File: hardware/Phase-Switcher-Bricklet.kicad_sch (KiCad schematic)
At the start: 42 parts, among them CN1 HC-GH-7PWTKK, P1 WJ124-3.81-2P, P2 WJ124-3.81-6P, P3 WJ124-3.81-6P, U1 XMC1302-Q024X0032-AB, U2 AQY282SX, U3 AQH3213A, U4 HCPL2731S, U5 AQH3213A, U6 HCPL2731S

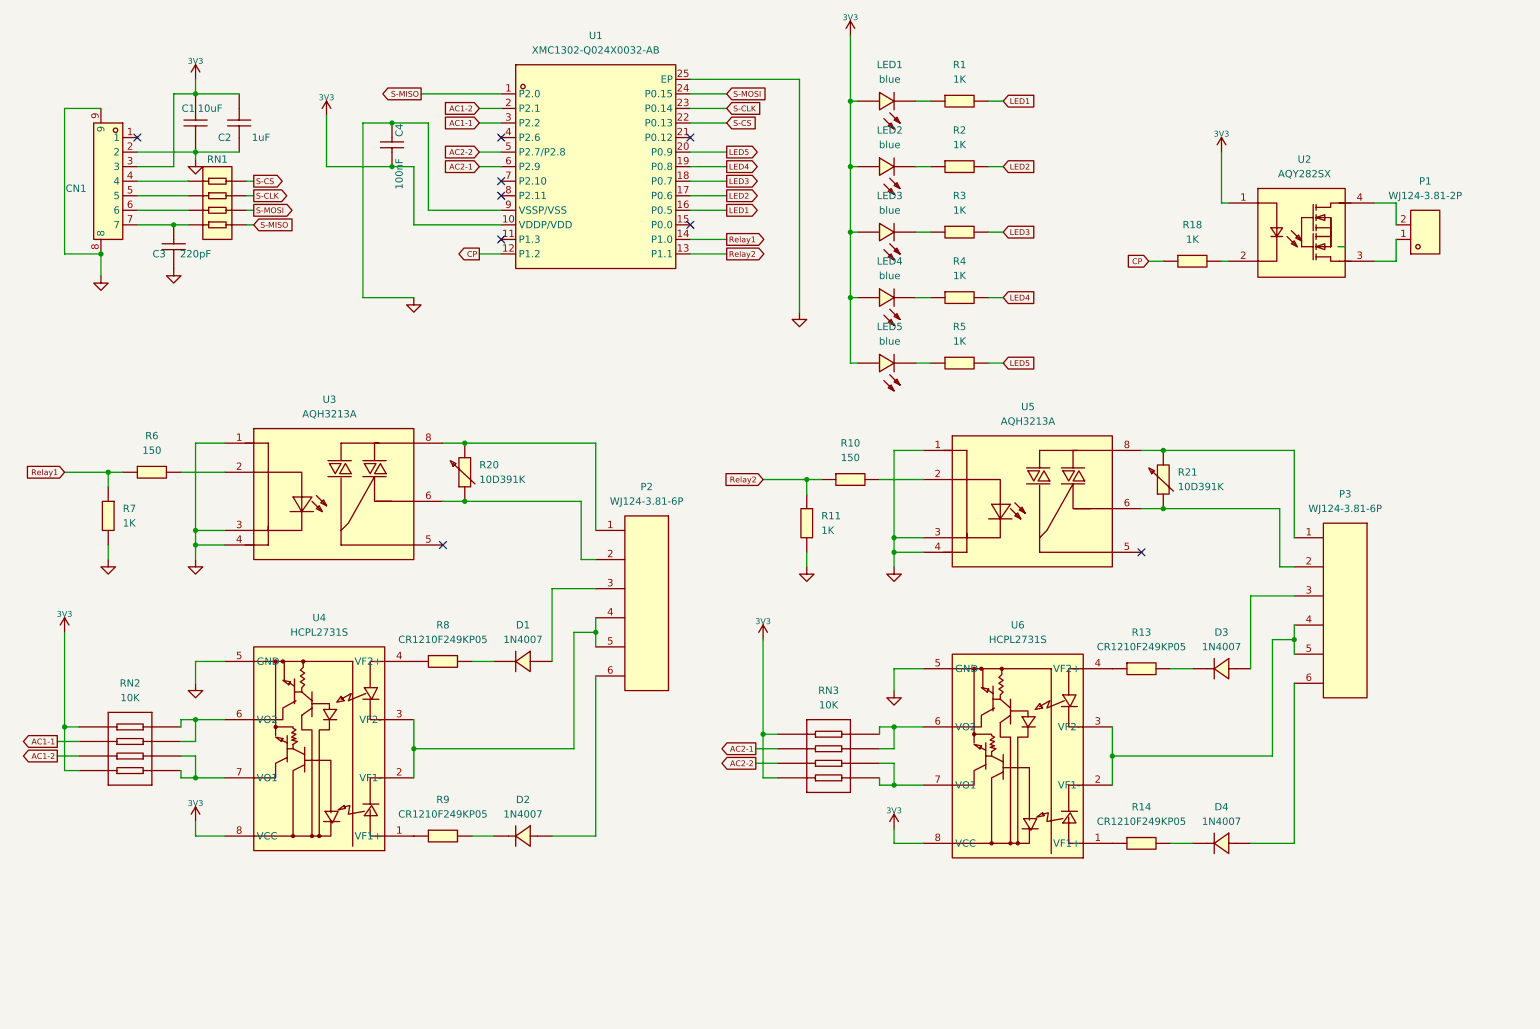
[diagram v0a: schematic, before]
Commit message: Phase-Switcher-Bricklet: Rev. 1.1
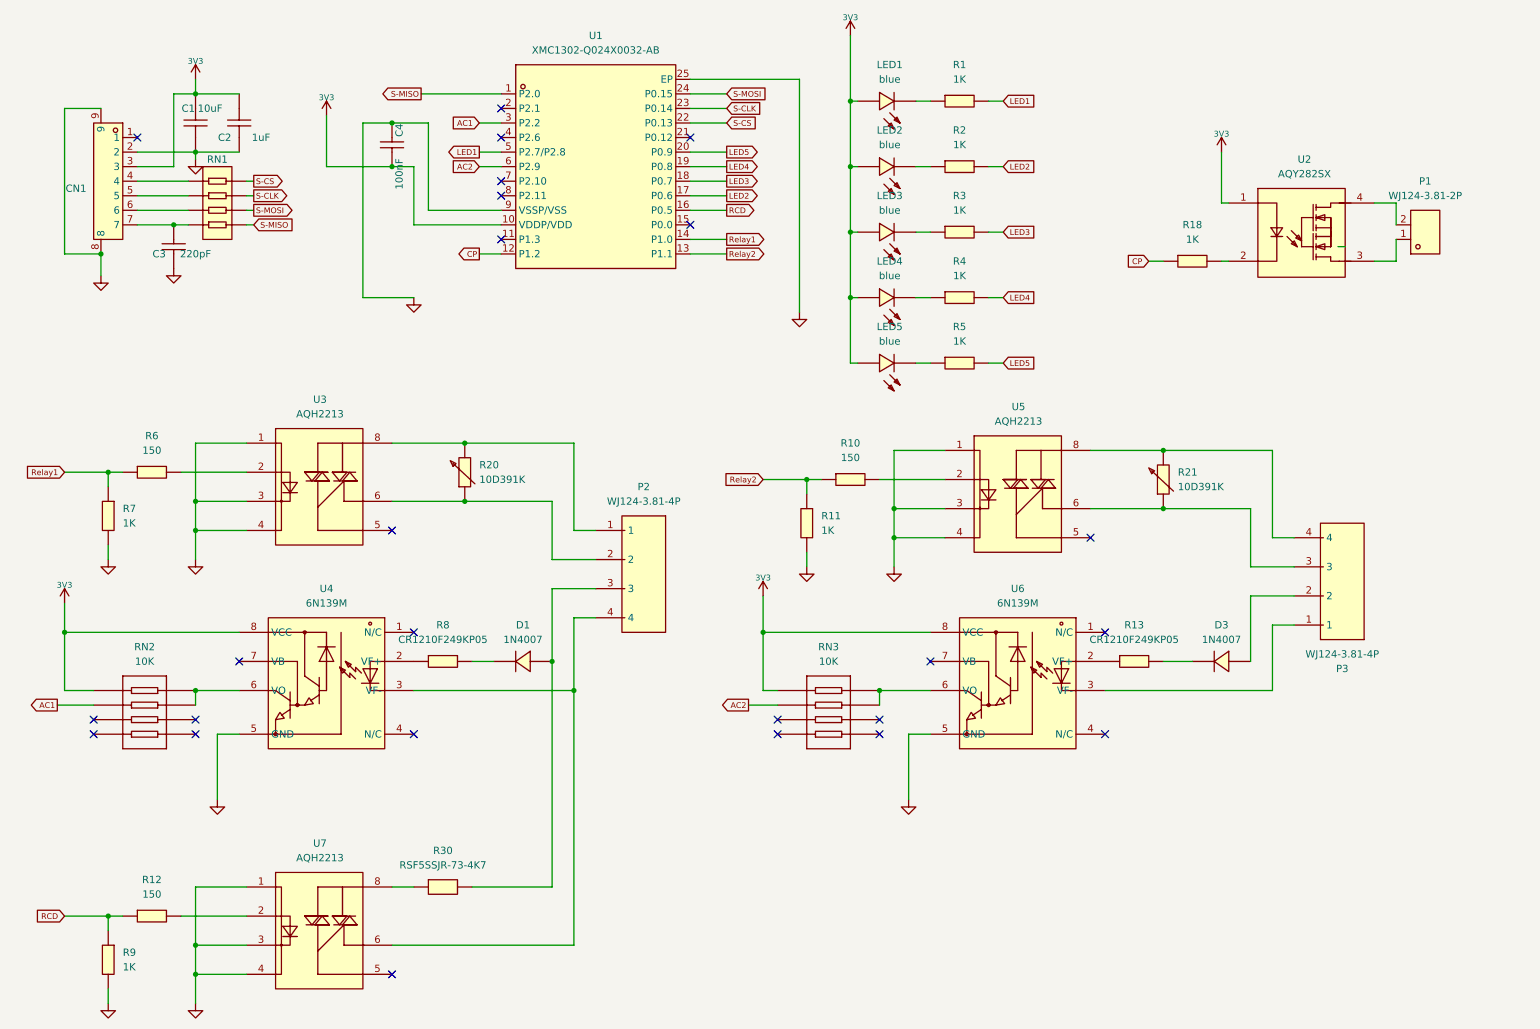
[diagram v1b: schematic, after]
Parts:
- removed D2, D4: 1N4007, easyeda2kicad:SOD-123FL_L2.8-W1.8-LS3.7-RD, symbol easyeda2kicad:1N4007A7
- removed P2, P3: WJ124-3.81-6P, easyeda2kicad:CONN-TH_6P-P3.81_WJ124-3.81-6P, symbol easyeda2kicad:WJ124-3.81-6P
- removed R14, R9: CR1210F249KP05, easyeda2kicad:R1210, symbol easyeda2kicad:CR1210F249KP05
- removed U3, U5: AQH3213A, easyeda2kicad:SMD-8_7P-L9.8-W6.4-P2.54-BL-PE7, symbol easyeda2kicad:AQH3213A
- removed U4, U6: HCPL2731S, easyeda2kicad:SMD-8_L9.8-W6.6-P2.54-LS10.3-BL, symbol easyeda2kicad:HCPL2731S
- added P2, P3: WJ124-3.81-4P, easyeda2kicad:CONN-TH_4P-P3.81_KF124-3.81-4P, symbol easyeda2kicad:WJ124-3.81-4P
- added R12: 150, easyeda2kicad:R0603, symbol easyeda2kicad:RC0603FR-07150RL
- added R30: RSF5SSJR-73-4K7, easyeda2kicad:RES-TH_BD6.5-L17.5-P21.50-D0.6, symbol easyeda2kicad:RSF5SSJR-73-4K7
- added R9: 1K, easyeda2kicad:R0603, symbol easyeda2kicad:Resistor-0603-1K
- added U3, U5, U7: AQH2213, easyeda2kicad:DIP-8_7P-L9.7-W6.4-P2.54-LS7.6-BL-PE7, symbol easyeda2kicad:AQH2213
- added U4, U6: 6N139M, easyeda2kicad:DIP-8_L9.4-W6.4-P2.54-LS9.1-BL, symbol easyeda2kicad:6N139M
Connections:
- net 3V3: now also U4.8 (VCC), U6.8 (VCC); no longer RN2.8, RN3.8
- net GND: now also R9.2, U3.1 (C), U3.3 (C), U3.4 (C), U4.5 (GND), U5.1 (C), U5.3 (C), U5.4 (C), U6.5 (GND), U7.1 (C), U7.3 (C), U7.4 (C)
- net LED1: now also U1.5 (P2.7/P2.8); no longer U1.16 (P0.5)
- net at R10.2: now also U5.2 (A)
- net at R21.1: now also P3.3, U5.6 (TT)
- net at R21.2: now also P3.4, U5.8 (TT)
- net at R20.2: now also P2.1, U3.8 (TT)
- net at R20.1: now also P2.2, U3.6 (TT)
- net at D1.2 (A): now also P2.3, R30.2
- net at RN3.1: no longer RN3.2
- net at RN3.3, RN3.4: now also U6.6 (VO)
- net at R6.2: now also U3.2 (A)
- net at R13.1: now also U6.2 (VF+)
- net at R8.1: now also U4.2 (VF+)
- net at D3.2 (A): now also P3.2
- net at RN2.3, RN2.4: now also U4.6 (VO)
- net at RN2.1: no longer RN2.2
- net AC1-1 renamed AC1
- net AC1-2: no longer names the net of U1.2 (P2.1)
- net AC1-2: no longer RN2.7
- net AC2-1 renamed AC2
- net AC2-2: no longer names the net of RN3.7
- net AC2-2: no longer U1.5 (P2.7/P2.8)
- new net: R12.2, U7.2 (A)
- new net: P2.4, U4.3 (VF-), U7.6 (TT)
- new net: R30.1, U7.8 (TT)
- new net: P3.1, U6.3 (VF-)
- new net RCD: R12.1, R9.1, U1.16 (P0.5)
- no-connect marks 9 -> 25
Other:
- moved on the sheet: D3, R13, RN2, RN3

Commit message: Phase-Switcher-Bricklet: Rev. 1.1a
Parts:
- removed RN3: 10K, easyeda2kicad:RES-ARRAY-SMD_0603-8P-L3.2-W1.6-BL, symbol easyeda2kicad:WA06X1002FTL
- removed U3, U5, U7: AQH2213, easyeda2kicad:DIP-8_7P-L9.7-W6.4-P2.54-LS7.6-BL-PE7, symbol easyeda2kicad:AQH2213
- added LED6: blue, easyeda2kicad:LED0603-RD, symbol easyeda2kicad:FC-DA1608BK-470H10
- added R6: 1K, easyeda2kicad:R0603, symbol easyeda2kicad:Resistor-0603-1K
- added U10, U20, U30: AQH2223, easyeda2kicad:DIP-8_7P-L9.7-W6.4-P2.54-LS7.6-BL-PE7, symbol easyeda2kicad:AQH2223
- renumbered D1 to D10, D3 to D20, P2 to P10, P3 to P20, P1 to P40, R7 to R10, R6 to R11, R20 to R12, R8 to R13, R11 to R20, R10 to R21, R21 to R22, R13 to R23, R9 to R30, R12 to R31, R30 to R32, R18 to R40, U4 to U11, U6 to U21, U2 to U40
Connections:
- net 3V3: now also RN2.7, LED6.2 (+)
- net AC2: now also RN2.8
- net GND: now also U10.1, U10.3, U10.4, U20.1, U20.3, U20.4, U30.1, U30.3, U30.4
- net LED1: now also U1.16 (P0.5); no longer U1.5 (P2.7/P2.8)
- net RCD: now also U1.11 (P1.3); no longer U1.16 (P0.5)
- net at R21.2: now also U20.2
- net at R22.1: now also P20.2, U20.6; no longer P20.3
- net at R22.2: now also P20.1, U20.8; no longer P20.4
- net AC2-1: now reaches U21.6 (VO)
- net AC2-1: now also RN2.1, RN2.2
- net at D10.2 (A), R32.2: now also P10.2; no longer P10.3
- net at R11.2: now also U10.2
- net at R12.1: now also P10.4, U10.6; no longer P10.2
- net at R12.2: now also P10.3, U10.8; no longer P10.1
- net at R31.2: now also U30.2
- net at U11.3 (VF-): now also P10.1, U30.6; no longer P10.4
- net AC1-1: now reaches RN2.3, RN2.4, U11.6 (VO)
- net at R32.1: now also U30.8
- net LED6: now reaches U1.21 (P0.12)
- net LED6: now also R6.2
- net at D20.2 (A): now also P20.3; no longer P20.2
- net at U21.3 (VF-): now also P20.4; no longer P20.1
- new net: LED6.1 (-), R6.1
- no-connect marks 25 -> 16
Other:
- moved on the sheet: LED1, LED2, LED3, LED4, LED5, P10, P20, P40, R1, R2, R3, R32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

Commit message: Phase-Switcher-Bricklet: Rev. 1.2
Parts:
- removed P20: WJ124-3.81-4P, easyeda2kicad:CONN-TH_4P-P3.81_KF124-3.81-4P, symbol easyeda2kicad:WJ124-3.81-4P
- removed R30: 1K, easyeda2kicad:R0603, symbol easyeda2kicad:Resistor-0603-1K
- removed R31: 150, easyeda2kicad:R0603, symbol easyeda2kicad:RC0603FR-07150RL
- removed R32: RSF5SSJR-73-4K7, easyeda2kicad:RES-TH_BD6.5-L17.5-P21.50-D0.6, symbol easyeda2kicad:RSF5SSJR-73-4K7
- removed U30: AQH2223, easyeda2kicad:DIP-8_7P-L9.7-W6.4-P2.54-LS7.6-BL-PE7, symbol easyeda2kicad:AQH2223
- added P11, P12: WJ124-3.81-2P, easyeda2kicad:CONN-TH_2P-P3.81_KF124-3.81-2P, symbol easyeda2kicad:WJ124-3.81-2P
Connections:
- net CP: now also U1.15 (P0.0); no longer U1.12 (P1.2)
- net at R22.1, U20.6: now also P10.2, R12.2, U10.8
- net at R22.2, U20.8: now also P10.1
- net at D10.2 (A): now also P11.1; no longer P10.2
- net at U11.3 (VF-): now also P11.2; no longer P10.1
- net at D20.2 (A): now also P12.1
- net at U21.3 (VF-): now also P12.2
- net AC1-1: no longer names the net of RN2.3, RN2.4, U11.6 (VO)
- net AC2-1: no longer names the net of RN2.1, RN2.2, U21.6 (VO)
- net RCD: no longer names the net of U1.11 (P1.3)
- now unconnected: P10.3
- no-connect marks 16 -> 17
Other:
- moved on the sheet: D20, R23, RN2, U21

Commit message: Phase-Switcher-Bricklet: Rev. 1.3
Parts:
- removed R13, R23: CR1210F249KP05, easyeda2kicad:R1210, symbol easyeda2kicad:CR1210F249KP05
- added R13, R23: RN1/2WS249KΩFT/BA1, easyeda2kicad:RES-TH_BD2.2-L6.5-P10.50-D0.6, symbol easyeda2kicad:RN1_2WS249KΩFT_BA1
- renumbered P12 to P21, P40 to P30, R40 to R30, U40 to U30
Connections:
- net at D10.1 (K): now also R13.1
- net at U21.2 (VF+): now also R23.2
- net at D20.1 (K): now also R23.1
- net at U11.2 (VF+): now also R13.2
